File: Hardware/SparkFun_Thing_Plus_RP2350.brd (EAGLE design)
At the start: 22.9 x 58.4 mm, 161 parts, among them J1 THING_PLUS_LOGICAL, J3 QWIIC_RIGHT_ANGLE, J6 MICRO-SD-ATOM, Q1 100mA/20V/3.8Ω, U1 RP2350A, U2 RM2, U3 RT9080-33GJ5, U4 LM66200, U5 W25QXX128MBIT, U6 MCP73831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

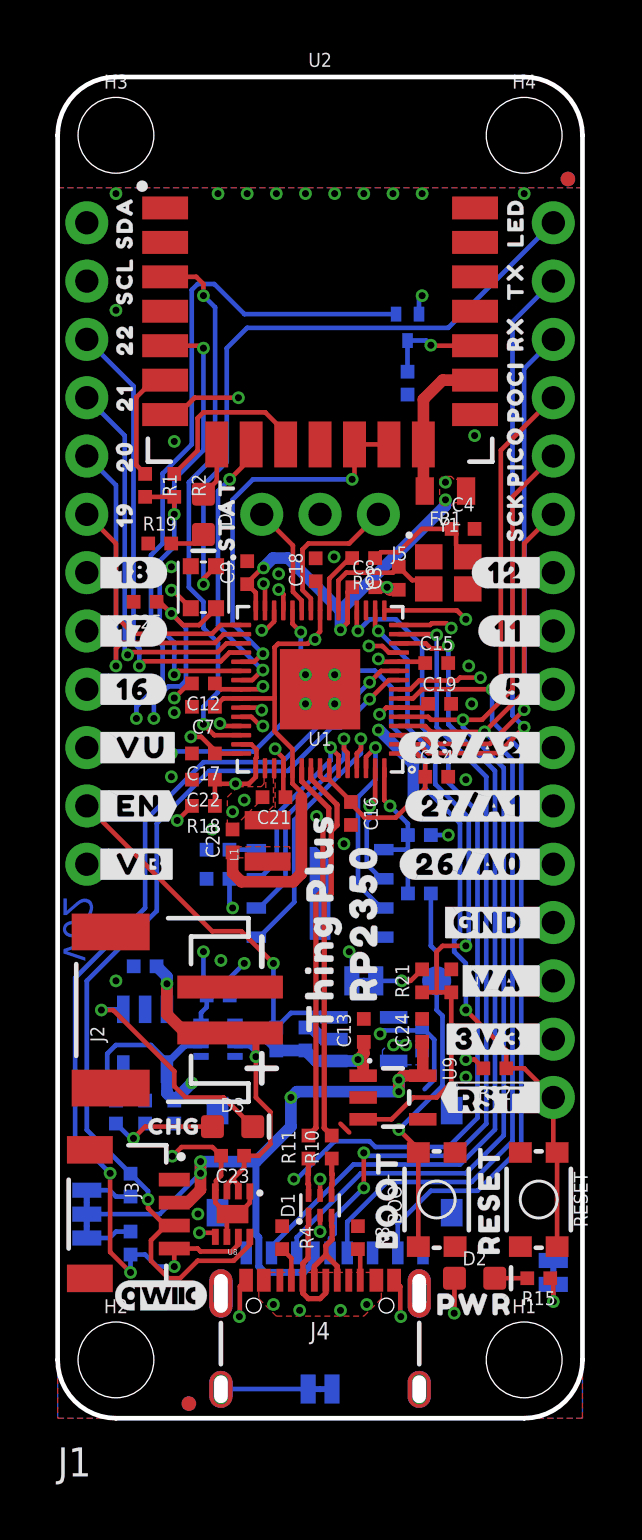
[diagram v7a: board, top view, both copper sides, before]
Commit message: Improve GND stitching
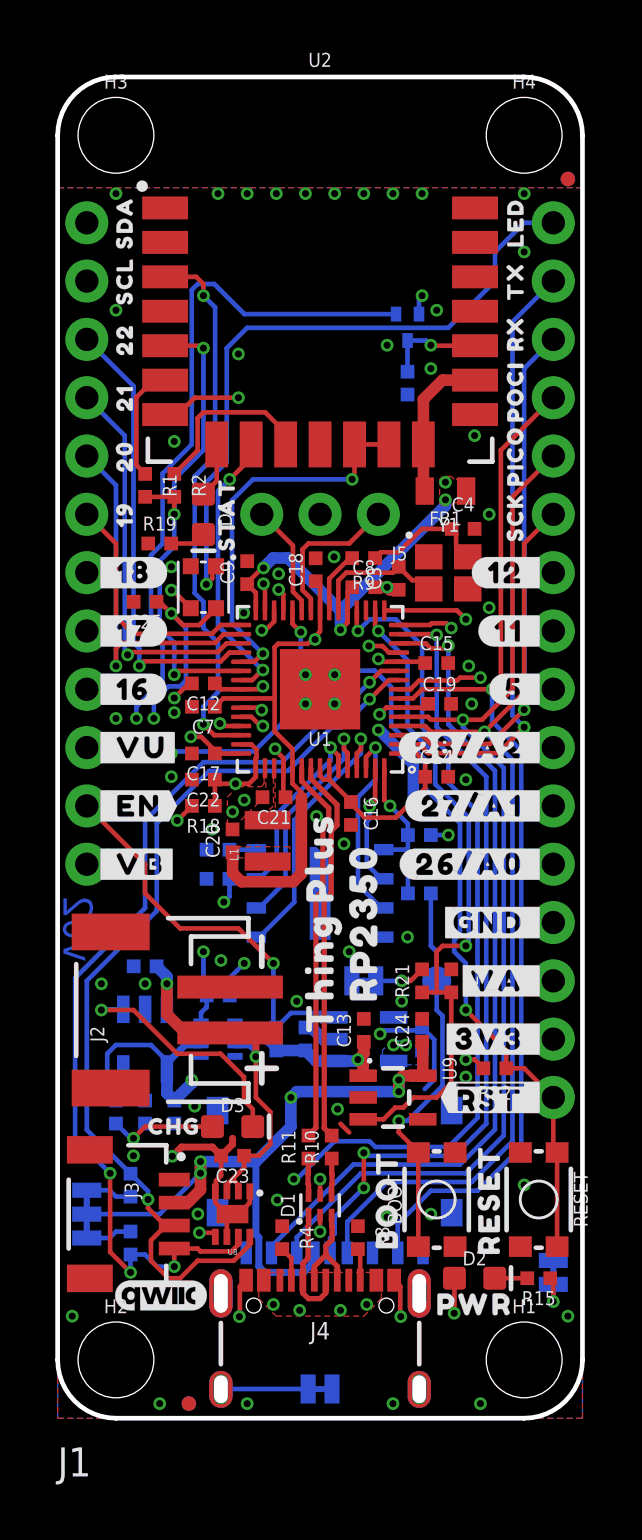
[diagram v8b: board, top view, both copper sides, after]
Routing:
- net GND: track 32.5 -> 35.9 mm, vias 43 -> 69
- net EN: track 16.7 -> 17.4 mm
- net N$22: track 10.0 -> 10.7 mm
- net LED_OUT: track 28.2 -> 28.8 mm
